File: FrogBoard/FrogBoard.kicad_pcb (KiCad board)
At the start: 2 copper layers, 59.3 x 50.6 mm, 33 parts, among them J1 Conn_01x10, J2 Conn_01x04, J3 USB_B_Micro, J4 Stickbox, U1 STM32L432KBUx, U2 USBLC6-2P6, U3 MCP1700T-3302E, U4 EMS3900

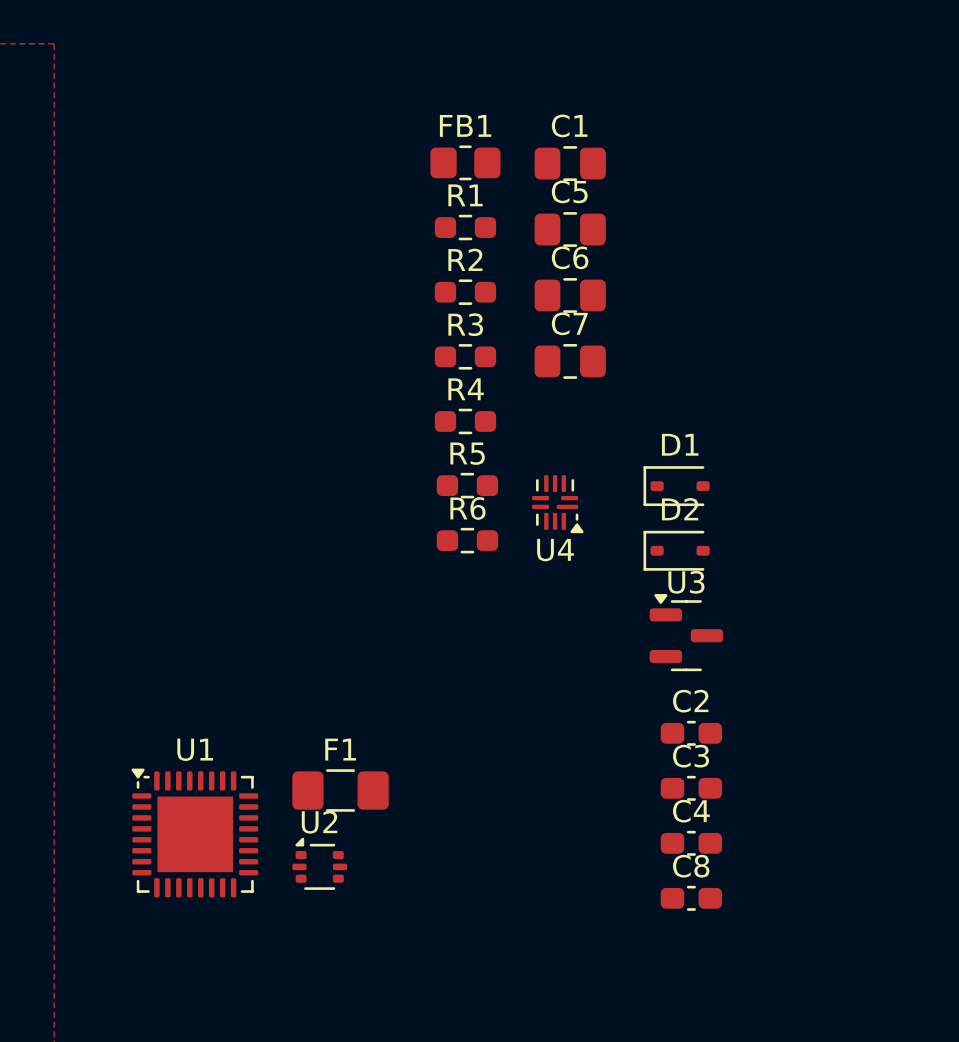
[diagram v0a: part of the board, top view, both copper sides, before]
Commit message: Cleaned up power filtering, fixed broken symbol and foorpting for mux, and started layout work
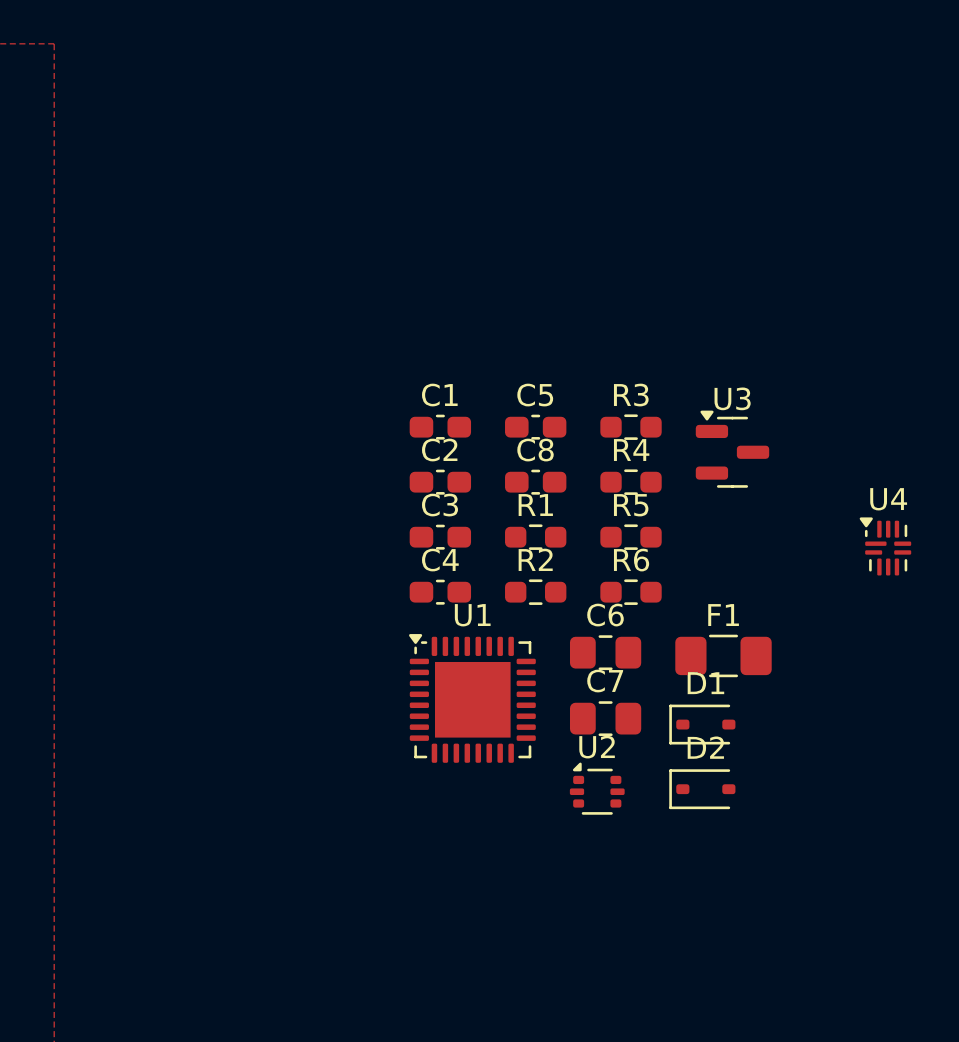
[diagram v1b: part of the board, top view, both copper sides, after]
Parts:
- removed FB1: 120R, Resistor_SMD:R_0805_2012Metric_Pad1.20x1.40mm_HandSolder
- C1: value 10uF -> 100nF; footprint Capacitor_SMD:C_0805_2012Metric_Pad1.18x1.45mm_HandSolder -> Capacitor_SMD:C_0603_1608Metric_Pad1.08x0.95mm_HandSolder
- C5: value 1uF -> 100nF; footprint Capacitor_SMD:C_0805_2012Metric_Pad1.18x1.45mm_HandSolder -> Capacitor_SMD:C_0603_1608Metric_Pad1.08x0.95mm_HandSolder
- moved C8 20.3 mm to (215.7, 89.2)
- moved F1 18.5 mm to (224.3, 97.1)
- moved C6 16.4 mm to (218.9, 97.0)
- moved C7 16.4 mm to (218.9, 100.0)
- moved C2 16.2 mm to (211.4, 89.2)
- moved C3 16.2 mm to (211.4, 91.7)
- moved C4 16.2 mm to (211.4, 94.2)
- moved U4 15.3 mm to (231.8, 92.2), turned to 0 degrees
- moved R1 14.5 mm to (215.7, 91.7)
- moved U1 14.1 mm to (212.8, 99.1)
- moved R2 14.1 mm to (215.7, 94.2)
- moved C1 13.4 mm to (211.4, 86.7)
- moved U2 13.1 mm to (218.5, 103.3)
- moved D1 10.9 mm to (223.5, 100.3)
- moved D2 10.9 mm to (223.5, 103.2)
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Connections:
- C4 pad 2: +3.3VA -> +3.3V
- R5 pad 1: Net-(U4-NO2) -> Net-(R5-Pad1)
- R6 pad 2: Net-(U4-NO2) -> Net-(R5-Pad1)
- U1 pad 5: +3.3VA -> +3.3V
- U4 pad 1: AX_MUX_OUT -> unconnected-(U4-COM1-Pad1)
- U4 pad 10: A_SEL -> unconnected-(U4-SEL-Pad10)
- U4 pad 2: AY_MUX_OUT -> unconnected-(U4-COM2-Pad2)
- U4 pad 3: GND -> unconnected-(U4-GND-Pad3)
- U4 pad 4: Net-(U4-NO2) -> unconnected-(U4-NC2-Pad4)
- U4 pad 5: AX_OUT -> unconnected-(U4-NC1-Pad5)
- U4 pad 6: AY_OUT -> unconnected-(U4-NO2-Pad6)
- U4 pad 7: Net-(U4-NO2) -> unconnected-(U4-NO1-Pad7)
- U4 pad 8: GND -> Net-(U4-GND-Pad11)
- U4 pad 9: +3.3V -> unconnected-(U4-VCC-Pad9)

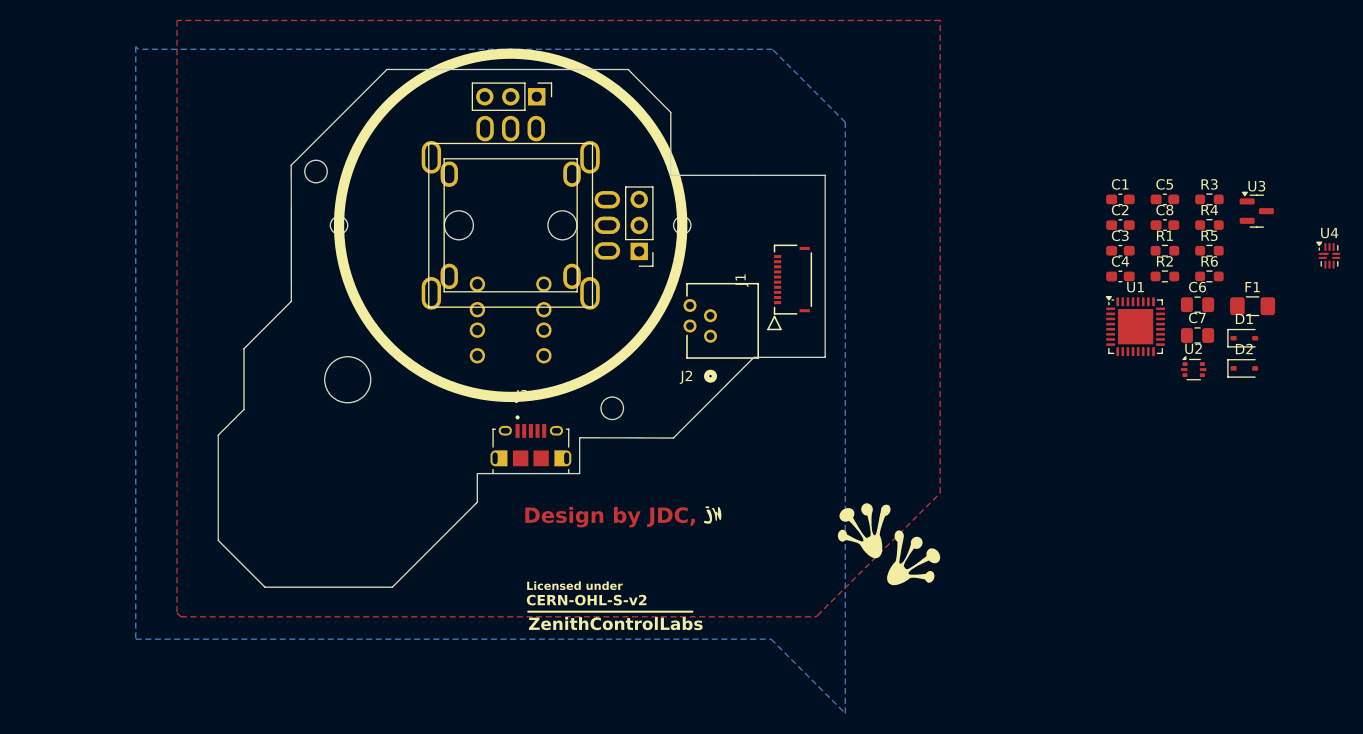
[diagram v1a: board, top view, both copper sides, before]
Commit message: routed the power section, places most ofthe components. Test points still to be added
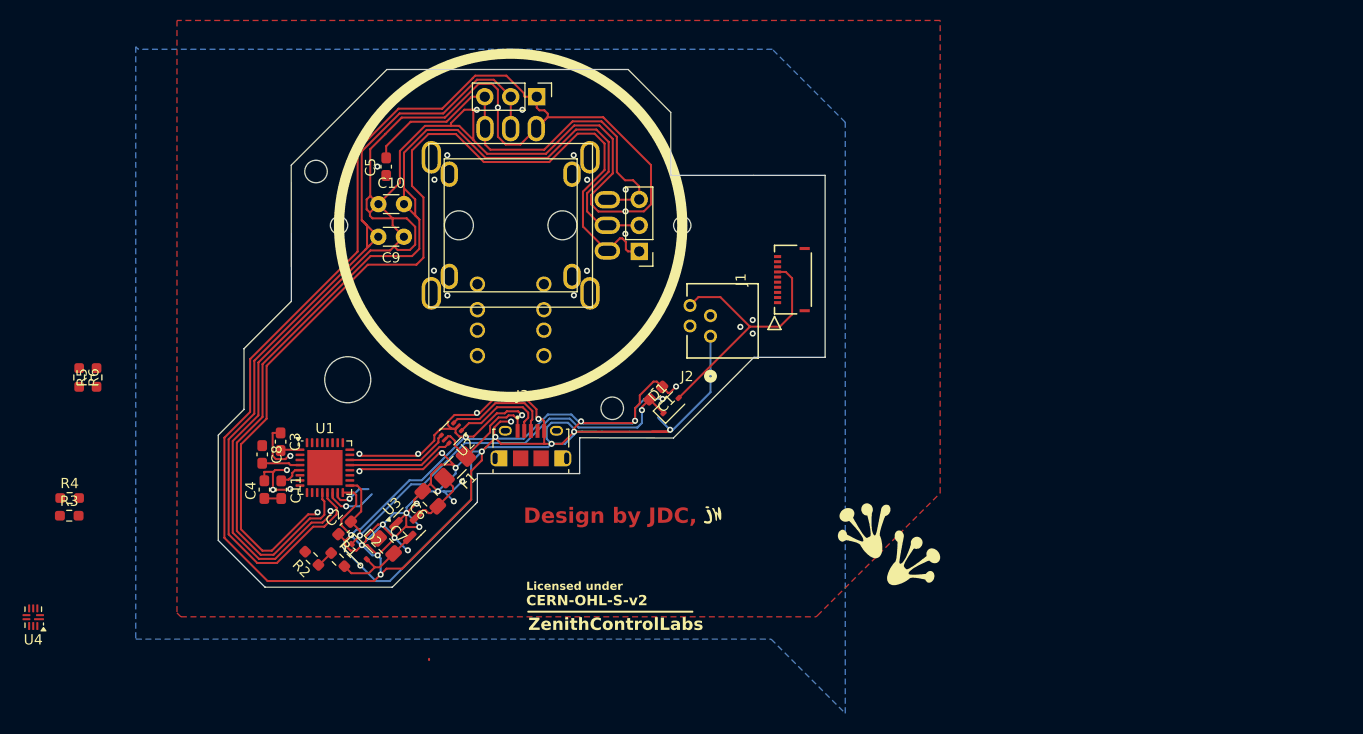
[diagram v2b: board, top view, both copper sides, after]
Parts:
- added C10: ~, Capacitor_THT:C_Disc_D3.0mm_W1.6mm_P2.50mm, F.Cu at (138.8, 87.2)
- added C11: 100nF, Capacitor_SMD:C_0603_1608Metric_Pad1.08x0.95mm_HandSolder, F.Cu at (129.3, 115.1)
- added C9: ~, Capacitor_THT:C_Disc_D3.0mm_W1.6mm_P2.50mm, F.Cu at (141.3, 90.3)
- moved U4 131.5 mm to (105.1, 127.5), turned to 180 degrees
- moved R3 115.7 mm to (108.6, 117.6)
- moved R4 114.6 mm to (108.6, 115.9)
- moved R6 110.9 mm to (109.6, 104.1), turned to -90 degrees
- moved R5 109.5 mm to (111.3, 104.1), turned to 90 degrees
- moved C8 91.0 mm to (127.5, 111.6), turned to -90 degrees
- moved D2 88.4 mm to (137.0, 121.1), turned to -45 degrees
- moved U3 88.3 mm to (141.9, 118.4), turned to 45 degrees
- moved R2 87.8 mm to (132.3, 121.8), turned to 135 degrees
- moved R1 86.3 mm to (134.9, 121.9), turned to -45 degrees
- moved C4 86.2 mm to (127.7, 115.1), turned to -90 degrees
- moved C3 84.2 mm to (129.3, 110.4), turned to -90 degrees
- moved C7 81.9 mm to (139.6, 120.6), turned to -45 degrees
- moved C2 81.4 mm to (135.5, 118.8), turned to 45 degrees
- moved U1 80.4 mm to (133.6, 112.9)
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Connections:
- J4 pad 3: +3.3VA -> +3.3V
- R5 pad 1: Net-(R5-Pad1) -> Net-(U4-NC1)
- R6 pad 2: Net-(R5-Pad1) -> Net-(U4-NC1)
- U1 pad 12: AX_IN -> AY_IN
- U1 pad 13: AY_IN -> AX_IN
- U1 pad 5: +3.3V -> Net-(U1-VDDA)
- U4 pad 1: unconnected-(U4-COM1-Pad1) -> AX_MUX_OUT
- U4 pad 10: unconnected-(U4-SEL-Pad10) -> A_SEL
- U4 pad 2: unconnected-(U4-COM2-Pad2) -> AY_MUX_OUT
- U4 pad 3: unconnected-(U4-GND-Pad3) -> GND
- U4 pad 4: unconnected-(U4-NC2-Pad4) -> Net-(U4-NC1)
- U4 pad 5: unconnected-(U4-NC1-Pad5) -> Net-(U4-NC1)
- U4 pad 6: unconnected-(U4-NO2-Pad6) -> AY_OUT
- U4 pad 7: unconnected-(U4-NO1-Pad7) -> AX_OUT
- U4 pad 8: Net-(U4-GND-Pad11) -> GND
- U4 pad 9: unconnected-(U4-VCC-Pad9) -> +3.3V
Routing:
- net GND: track 0.00 -> 625.8 mm, vias 0 -> 57
- net AY_IN: track 0.00 -> 101.6 mm
- net +3.3V: track 0.00 -> 91.6 mm, vias 0 -> 2
- net AX_IN: track 0.00 -> 85.1 mm
- net +3.3V_HORI: track 0.00 -> 27.1 mm
- net VBUS: track 0.00 -> 11.7 mm
- net /USB_RAW+: track 0.00 -> 10.8 mm
- net USB-: track 0.00 -> 10.6 mm
- net USB+: track 0.00 -> 10.2 mm
- net /USB_RAW-: track 0.00 -> 9.66 mm
- net +3.3V_USB: track 0.00 -> 9.23 mm
- net Net-(U3-VI): track 0.00 -> 6.50 mm
- net FFC_P2: track 0.00 -> 5.19 mm, vias 0 -> 1
- net FFC_P3: track 0.00 -> 4.03 mm, vias 0 -> 1
- net Net-(U1-NRST): track 0.00 -> 3.77 mm
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
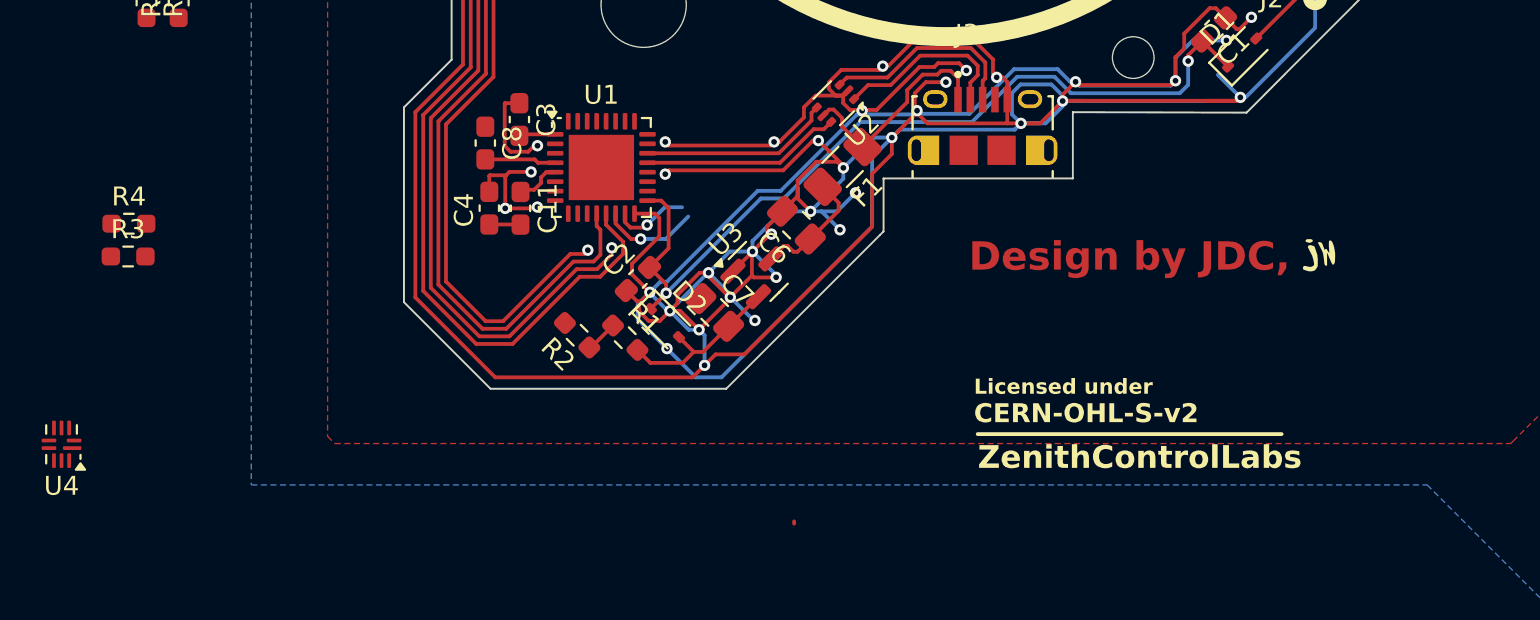
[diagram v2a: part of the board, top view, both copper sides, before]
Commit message: Switch to BL1555 analog chip
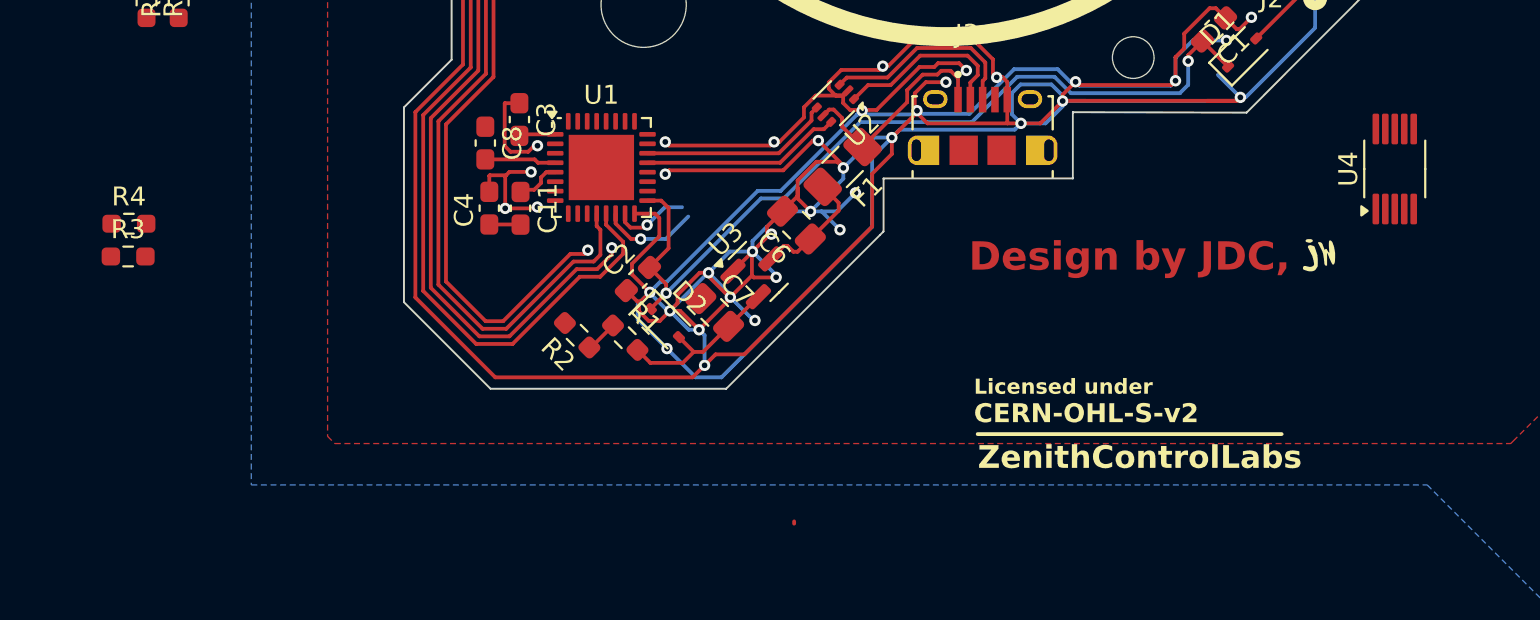
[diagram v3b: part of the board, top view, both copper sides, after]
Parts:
- U4: value EMS3900 -> BL1555; footprint Package_DFN_QFN:UQFN-10_1.4x1.8mm_P0.4mm -> Package_SO:MSOP-10_3x3mm_P0.5mm
- moved U4 71.9 mm to (175.5, 113.0), turned to 90 degrees
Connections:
- R5 pad 1: Net-(U4-NC1) -> /A_MID
- R6 pad 2: Net-(U4-NC1) -> /A_MID
- U4 pad 1: AX_MUX_OUT -> +3.3V
- U4 pad 10: A_SEL -> AY_OUT
- U4 pad 2: AY_MUX_OUT -> AX_OUT
- U4 pad 3: GND -> AX_MUX_OUT
- U4 pad 4: Net-(U4-NC1) -> A_SEL
- U4 pad 5: Net-(U4-NC1) -> /A_MID
- U4 pad 6: AY_OUT -> GND
- U4 pad 7: AX_OUT -> /A_MID
- U4 pad 8: GND -> A_SEL
- U4 pad 9: +3.3V -> AY_MUX_OUT

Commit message: first pass at layout
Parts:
- added J5: Conn_01x03_Socket, Connector_PinHeader_1.00mm:PinHeader_1x03_P1.00mm_Vertical, F.Cu at (127.0, 121.6)
- moved R6 69.8 mm to (177.1, 86.4), turned to 180 degrees
- moved R5 67.8 mm to (177.1, 88.0), turned to 0 degrees
- moved C4 59.0 mm to (179.6, 87.1)
- moved R4 23.5 mm to (130.2, 106.5), turned to -90 degrees
- moved U4 23.2 mm to (172.7, 89.9), turned to -90 degrees
- moved R3 22.7 mm to (128.7, 107.0), turned to -90 degrees
- moved C8 1.77 mm to (128.7, 112.9), turned to 0 degrees
- moved C3 1.25 mm to (128.3, 111.2), turned to 0 degrees
- moved C11 0.31 mm to (129.2, 115.4)
- moved U2 0.06 mm to (146.0, 109.6)
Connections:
- net Net-(U1-PH3) renamed BOOT_SEL
- C11 pad 1: +3.3V -> GND
- C11 pad 2: Net-(U1-VDDA) -> +3.3V
- U1 pad 14: FFC_P2 -> FFC_P6
- U1 pad 15: FFC_P3 -> FFC_P5
- U1 pad 27: FFC_P5 -> FFC_P2
- U1 pad 28: FFC_P6 -> FFC_P3
- U1 pad 5: Net-(U1-VDDA) -> +3.3V
- U4 pad 10: AY_OUT -> AX_OUT
- U4 pad 2: AX_OUT -> AY_OUT
- U4 pad 3: AX_MUX_OUT -> AY_MUX_OUT
- U4 pad 9: AY_MUX_OUT -> AX_MUX_OUT
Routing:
- net GND: track 625.8 -> 1476.7 mm, vias 57 -> 185
- net +3.3V: track 91.6 -> 242.0 mm, vias 2 -> 10
- net SDA: track 0.00 -> 74.8 mm
- net FFC_P6: track 0.00 -> 67.7 mm, vias 0 -> 2
- net SCL: track 0.00 -> 67.6 mm
- net FFC_P5: track 0.00 -> 65.6 mm, vias 0 -> 2
- net STICK_BTN: track 0.00 -> 61.9 mm, vias 0 -> 2
- net AY_OUT: track 0.00 -> 61.0 mm, vias 0 -> 2
- net A_SEL: track 0.00 -> 60.9 mm, vias 0 -> 2
- net AX_OUT: track 0.00 -> 59.2 mm, vias 0 -> 2
- net FFC_P4: track 0.00 -> 55.4 mm, vias 0 -> 2
- net FFC_P3: track 4.03 -> 55.3 mm, vias 1 -> 0
- net FFC_P2: track 5.19 -> 54.5 mm, vias 1 -> 0
- net BOOT_SEL: track 1.74 -> 27.7 mm, vias 0 -> 2
- net AY_MUX_OUT: track 0.00 -> 15.3 mm
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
